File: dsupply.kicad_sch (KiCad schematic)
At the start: 55 parts, among them J5 Barrel_Jack_MountingPin, Q2 BSS138, Q3 BSS138, Q4 BC857, Q5 AOSP21321, Q6 BC857, U21 ACPL-217-500E, U22 TPS54620, U23 AG5300, U24 ACPL-217-500E, U25 AMS1117-3.3

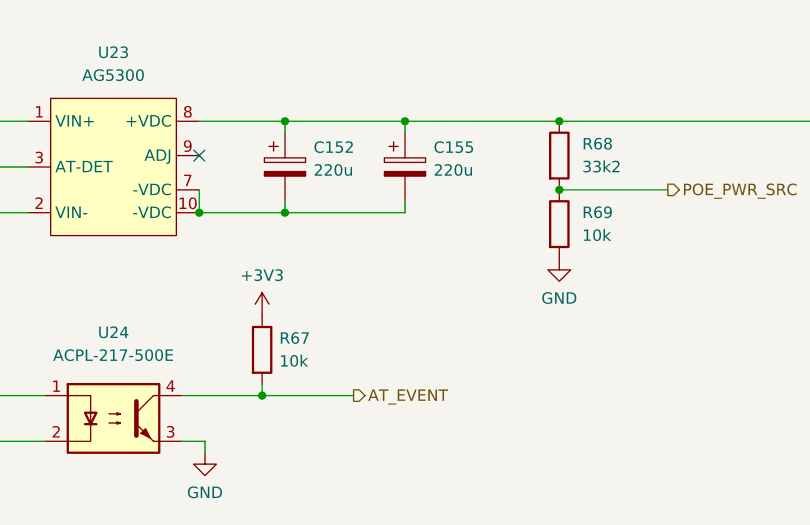
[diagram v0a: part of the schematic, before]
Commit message: add V01 production files, bug fixes
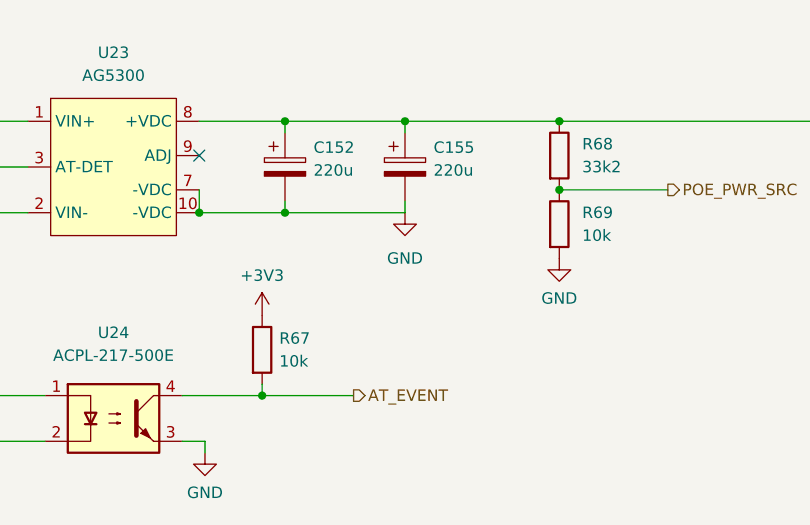
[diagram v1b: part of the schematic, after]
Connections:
- net GND: now also C152.2, C155.2, U23.10 (-VDC), U23.7 (-VDC)
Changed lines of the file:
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@@
     (pin "2")
+  )
+  (symbol (lib_id "power:GND") (at 231.14 86.36 0) (unit 1)
+    (in_bom yes) (on_board yes) (fields_autoplaced)
+    (property "Reference" "#PWR?" (id 0) (at 231.14 92.71 0)
+      (effects (font (size 1.27 1.27)) hide)
+    )
+    (property "Value" "GND" (id 1) (at 231.14 91.44 0))
+    (property "Footprint" "" (id 2) (at 231.14 86.36 0)
+      (effects (font (size 1.27 1.27)) hide)
+    )
+    (property "Datasheet" "" (id 3) (at 231.14 86.36 0)
+      (effects (font (size 1.27 1.27)) hide)
+    )
+    (pin "1")
   )
   (symbol (lib_id "power:PWR_FLAG") (at 177.8 86.36 0) (unit 1)

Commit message: v 0.2 schematics
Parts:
- removed C152: 220u, Capacitor_Tantalum_SMD:CP_EIA-7343-15_Kemet-W, symbol Device:C_Polarized
- removed J5: Barrel_Jack_MountingPin, Connector_BarrelJack:BarrelJack_CUI_PJ-063AH_Horizontal, symbol Connector:Barrel_Jack_MountingPin
- removed R67: 10k, Resistor_SMD:R_0603_1608Metric, symbol Device:R
- removed U24: ACPL-217-500E, Package_DIP:SMDIP-4_W7.62mm, symbol Isolator:SFH617A-2X009T
- added C? (x3): 10u, Capacitor_SMD:C_0805_2012Metric, symbol Device:C
- added C? (x2): 100n, Capacitor_SMD:C_0603_1608Metric, symbol Device:C
- added C? (x2): 220u, Capacitor_Tantalum_SMD:CP_EIA-7343-15_Kemet-W, symbol Device:C_Polarized
- added J5: Barrel_Jack, Connector_BarrelJack:BarrelJack_CUI_PJ-063AH_Horizontal, symbol Connector:Barrel_Jack
- added L? (x2): 1u, Inductor_SMD:L_1008_2520Metric, symbol Device:L
- added TP34, TP35: TestPoint, TestPoint:TestPoint_Pad_2.0x2.0mm, symbol Connector:TestPoint
- added U?: PM1202, kirdy:PM1202, symbol kirdy:PM1202
- R62: footprint Resistor_SMD:R_1206_3216Metric -> Resistor_SMD:R_0603_1608Metric; MFR_PN RNCP1206FTD10R0 -> RT0603BRD0710RL; MFR_PN_ALT CRM1206-FX-10R0ELF -> WR06X10R0FTL
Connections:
- net +12V: now also J5.1
- net +3V3: now also TP35.1
- net +5V: now also L?.1, TP34.1; no longer FB10.1
- net GND: now also C?.2, C?.2, C?.2, C?.2, C?.2, C?.2, C?.2, J5.2, U?.7 (-VDC), U?.8 (-VDC)
- net at C146.1, FL2.4, U23.1 (VIN+): now also U?.3 (VIN+)
- net at Q4.2 (E), Q5.5 (D), Q5.6 (D)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: now also C?.1, C?.1, C?.1, C?.1, L?.2; no longer C155.1, U23.8 (+VDC)
- net at C148.1, FL2.3, U23.2 (VIN-): now also U?.4 (VIN-)
- new net: C?.1, C?.1, C?.1, FB10.1, L?.2
- new net: C155.1, L?.1, U23.8 (+VDC), U?.10 (+VDC), U?.9 (+VDC)
- no-connect marks 2 -> 3
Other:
- note added: "ONLY POPULATE EITHER ONE!"
- moved on the sheet: C155, C158, C159, C160, C161, FB10, Q4, Q5, Q6, R68, R69, R70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

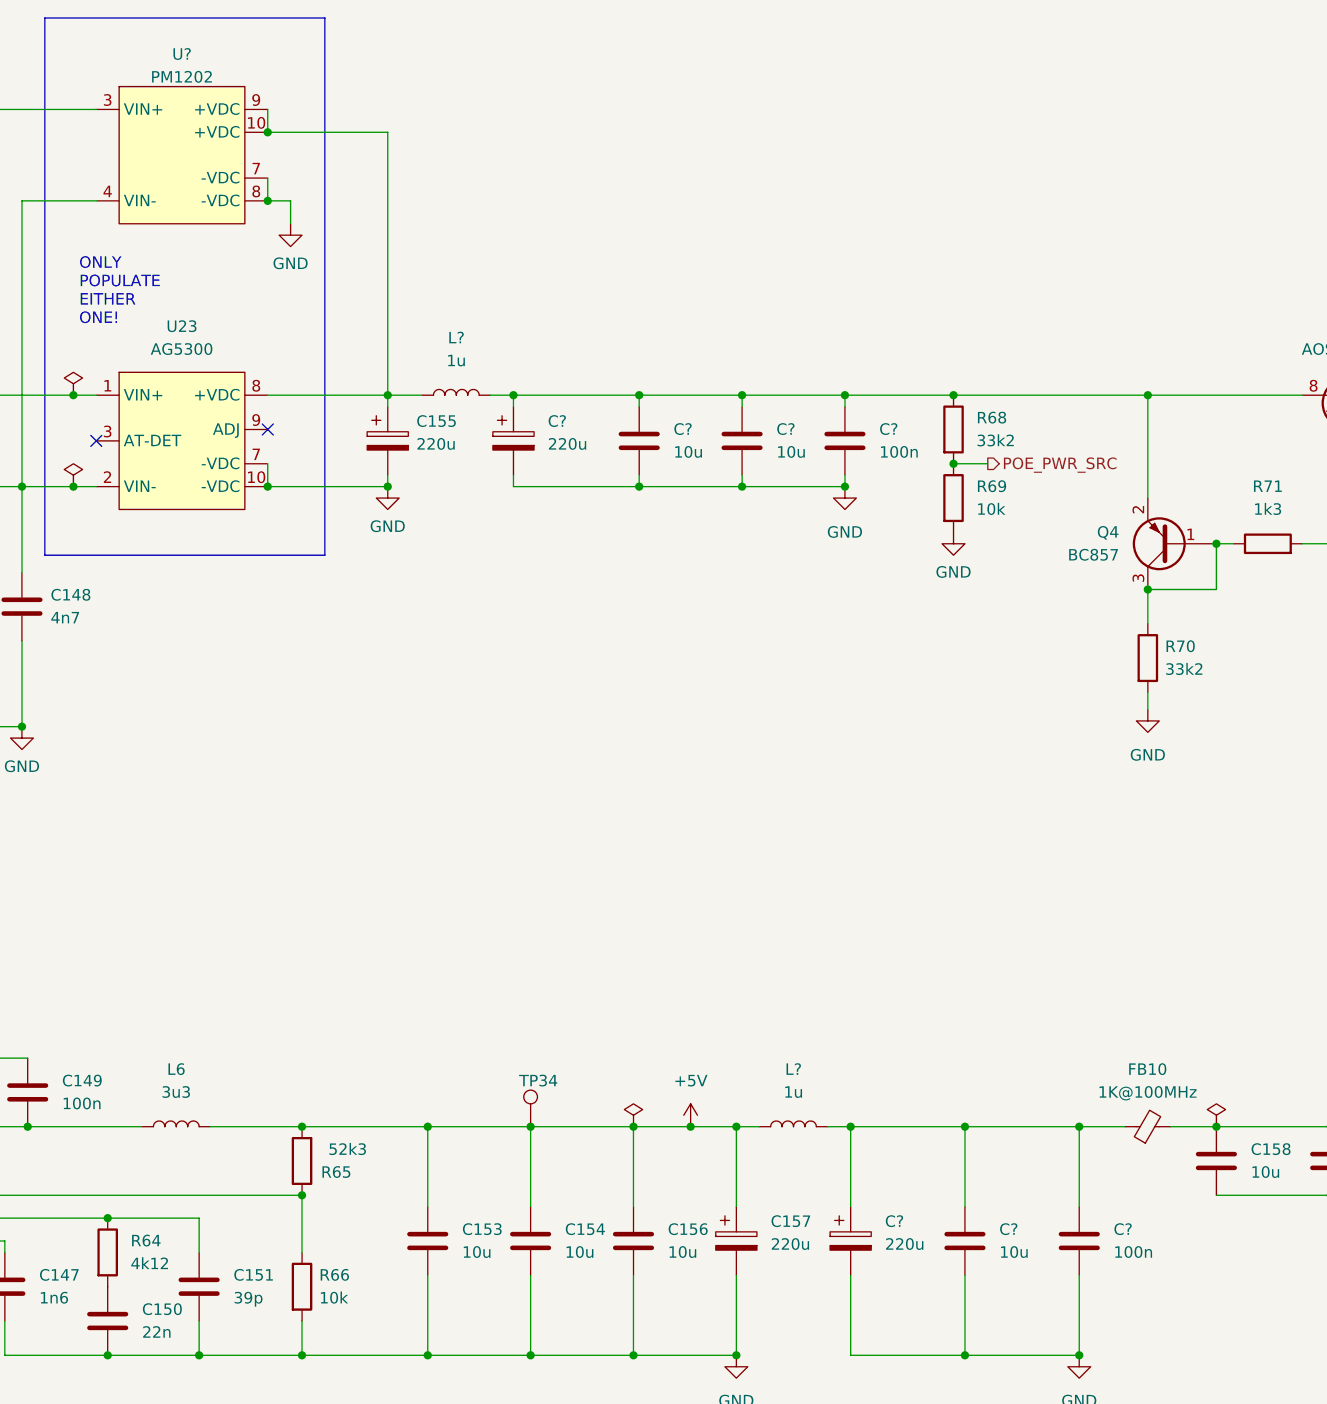
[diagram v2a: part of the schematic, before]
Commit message: change damper
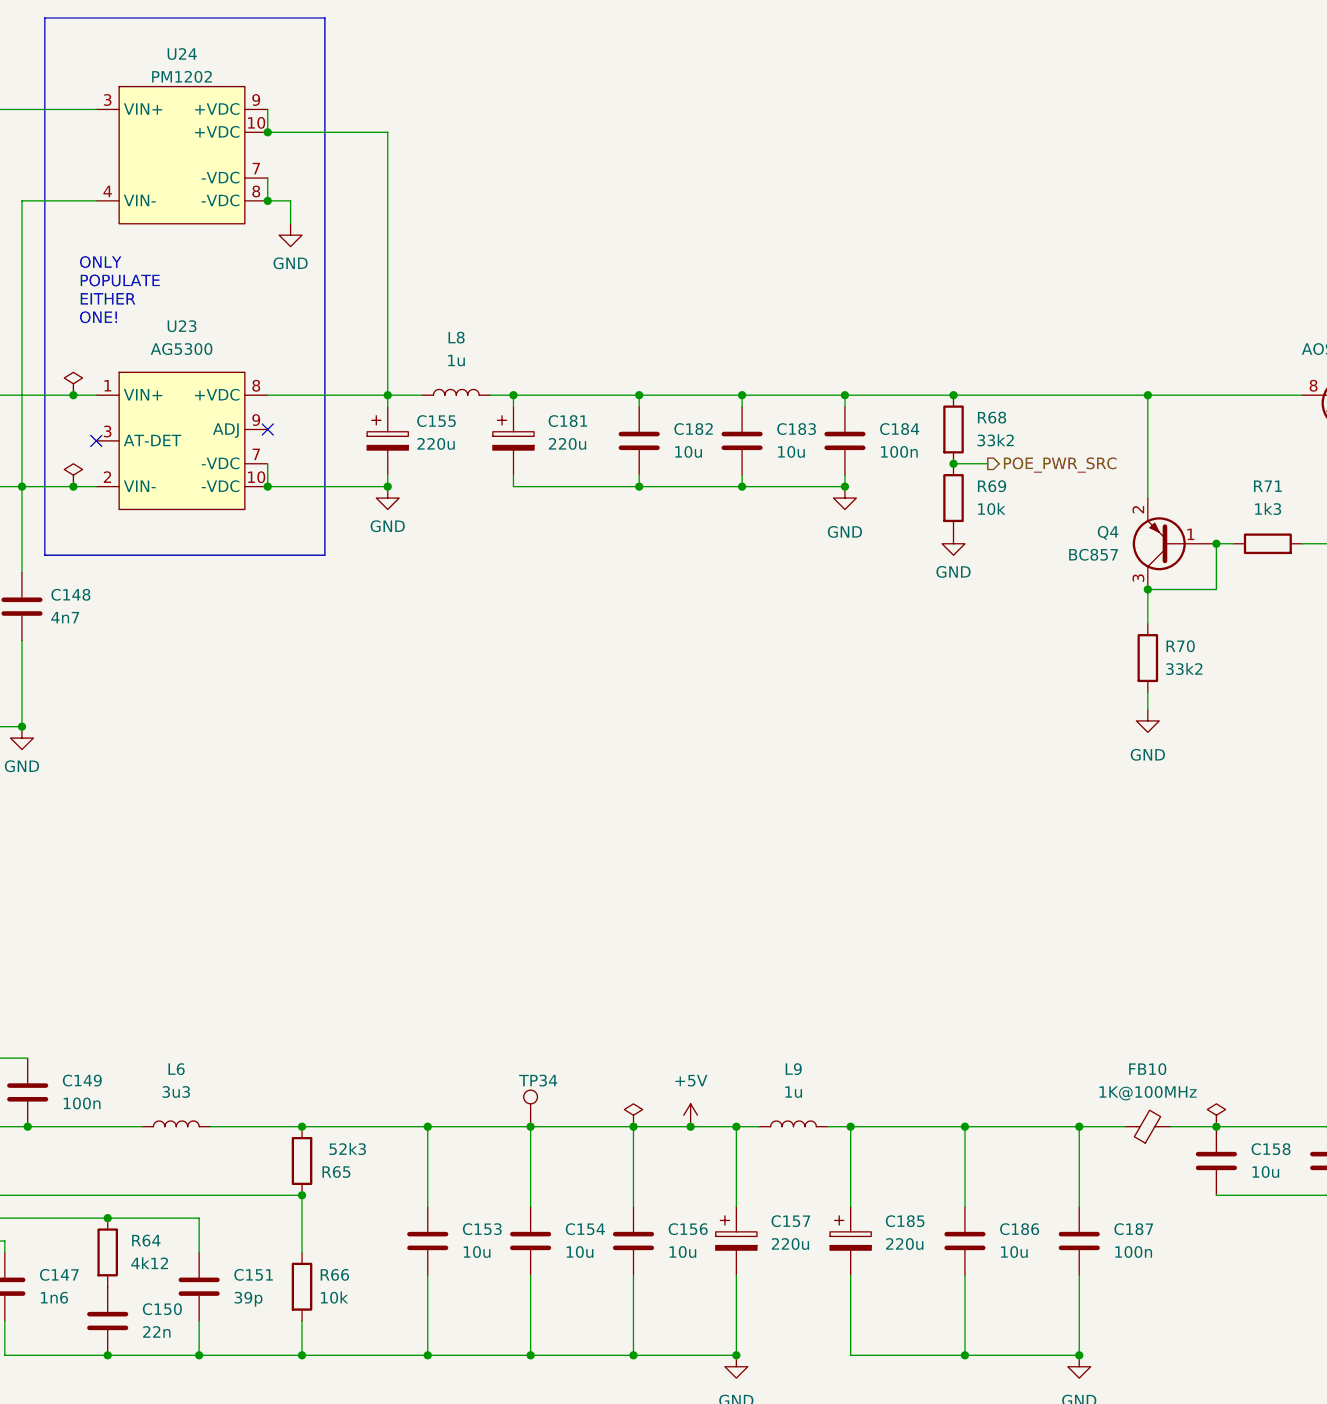
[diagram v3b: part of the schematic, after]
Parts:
- gave numbers to parts that had none: 10
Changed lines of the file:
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@@
   (symbol (lib_id "Device:C") (at 276.86 170.18 0) (unit 1)
     (in_bom yes) (on_board yes) (fields_autoplaced)
-    (property "Reference" "C?" (id 0) (at 280.67 168.9099 0)
+    (property "Reference" "C186" (id 0) (at 280.67 168.9099 0)
       (effects (font (size 1.27 1.27)) (justify left))
     )
@@
   (symbol (lib_id "Device:C") (at 263.525 81.28 0) (unit 1)
     (in_bom yes) (on_board yes) (fields_autoplaced)
-    (property "Reference" "C?" (id 0) (at 267.335 80.0099 0)
+    (property "Reference" "C184" (id 0) (at 267.335 80.0099 0)
       (effects (font (size 1.27 1.27)) (justify left))
     )
@@
   (symbol (lib_id "Device:C") (at 252.095 81.28 0) (unit 1)
     (in_bom yes) (on_board yes) (fields_autoplaced)
-    (property "Reference" "C?" (id 0) (at 255.905 80.0099 0)
+    (property "Reference" "C183" (id 0) (at 255.905 80.0099 0)
       (effects (font (size 1.27 1.27)) (justify left))
     )
@@
   (symbol (lib_id "Device:C_Polarized") (at 264.16 170.18 0) (unit 1)
     (in_bom yes) (on_board yes) (fields_autoplaced)
-    (property "Reference" "C?" (id 0) (at 267.97 168.0209 0)
+    (property "Reference" "C185" (id 0) (at 267.97 168.0209 0)
       (effects (font (size 1.27 1.27)) (justify left))
     )
@@
   (symbol (lib_id "Device:C_Polarized") (at 226.695 81.28 0) (unit 1)
     (in_bom yes) (on_board yes) (fields_autoplaced)
-    (property "Reference" "C?" (id 0) (at 230.505 79.1209 0)
+    (property "Reference" "C181" (id 0) (at 230.505 79.1209 0)
       (effects (font (size 1.27 1.27)) (justify left))
     )
@@
   (symbol (lib_id "kirdy:PM1202") (at 189.23 52.07 0) (unit 1)
     (in_bom yes) (on_board yes) (fields_autoplaced)
-    (property "Reference" "U?" (id 0) (at 189.865 38.3372 0))
+    (property "Reference" "U24" (id 0) (at 189.865 38.3372 0))
     (property "Value" "PM1202" (id 1) (at 189.865 40.8741 0))
     (property "Footprint" "kirdy:PM1202" (id 2) (at 167.64 36.83 0)
@@
   (symbol (lib_id "Device:C") (at 240.665 81.28 0) (unit 1)
     (in_bom yes) (on_board yes) (fields_autoplaced)
-    (property "Reference" "C?" (id 0) (at 244.475 80.0099 0)
+    (property "Reference" "C182" (id 0) (at 244.475 80.0099 0)
       (effects (font (size 1.27 1.27)) (justify left))
     )
@@
   (symbol (lib_id "Device:L") (at 257.81 157.48 90) (unit 1)
     (in_bom yes) (on_board yes) (fields_autoplaced)
-    (property "Reference" "L?" (id 0) (at 257.81 151.13 90))
+    (property "Reference" "L9" (id 0) (at 257.81 151.13 90))
     (property "Value" "1u" (id 1) (at 257.81 153.67 90))
     (property "Footprint" "Inductor_SMD:L_1008_2520Metric" (id 2) (at 257.81 157.48 0)
@@
   (symbol (lib_id "Device:C") (at 289.56 170.18 0) (unit 1)
     (in_bom yes) (on_board yes) (fields_autoplaced)
-    (property "Reference" "C?" (id 0) (at 293.37 168.9099 0)
+    (property "Reference" "C187" (id 0) (at 293.37 168.9099 0)
       (effects (font (size 1.27 1.27)) (justify left))
     )
@@
   (symbol (lib_id "power:GND") (at 212.725 86.36 0) (unit 1)
     (in_bom yes) (on_board yes) (fields_autoplaced)
-    (property "Reference" "#PWR?" (id 0) (at 212.725 92.71 0)
+    (property "Reference" "#PWR0166" (id 0) (at 212.725 92.71 0)
       (effects (font (size 1.27 1.27)) hide)
     )
@@
   (symbol (lib_id "power:GND") (at 263.525 86.36 0) (unit 1)
     (in_bom yes) (on_board yes) (fields_autoplaced)
-    (property "Reference" "#PWR?" (id 0) (at 263.525 92.71 0)
+    (property "Reference" "#PWR0167" (id 0) (at 263.525 92.71 0)
       (effects (font (size 1.27 1.27)) hide)
     )
@@
   (symbol (lib_id "power:GND") (at 201.93 57.15 0) (unit 1)
     (in_bom yes) (on_board yes) (fields_autoplaced)
-    (property "Reference" "#PWR?" (id 0) (at 201.93 63.5 0)
+    (property "Reference" "#PWR0165" (id 0) (at 201.93 63.5 0)
       (effects (font (size 1.27 1.27)) hide)
     )
@@
   (symbol (lib_id "Device:L") (at 220.345 76.2 90) (unit 1)
     (in_bom yes) (on_board yes) (fields_autoplaced)
-    (property "Reference" "L?" (id 0) (at 220.345 69.85 90))
+    (property "Reference" "L8" (id 0) (at 220.345 69.85 90))
     (property "Value" "1u" (id 1) (at 220.345 72.39 90))
     (property "Footprint" "Inductor_SMD:L_1008_2520Metric" (id 2) (at 220.345 76.2 0)
@@
   (symbol (lib_id "power:GND") (at 289.56 182.88 0) (unit 1)
     (in_bom yes) (on_board yes) (fields_autoplaced)
-    (property "Reference" "#PWR?" (id 0) (at 289.56 189.23 0)
-      (effects (font (size 1.27 1.27)) hide)
-    )
+    (property "Reference" "#PWR0168" (id 0) (at 289.56 189.23 0)
+      (effects (font (size 1.27 1.27)) hide)
+    )
